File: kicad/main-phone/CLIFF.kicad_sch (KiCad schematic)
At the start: 14 parts, among them Q7304 AO3400

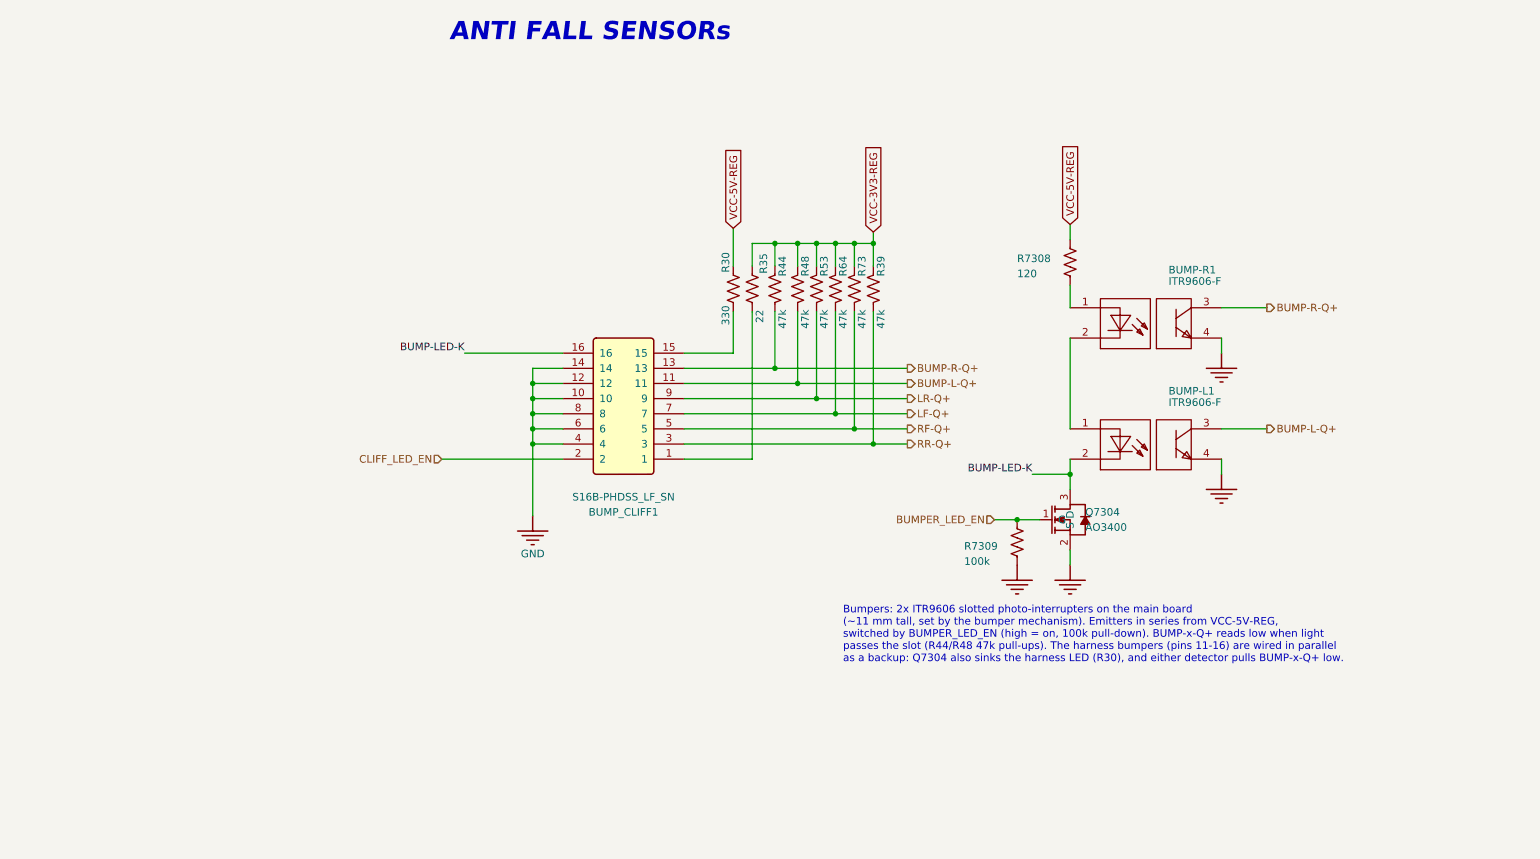
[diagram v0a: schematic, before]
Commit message: Cliff sensor board (IR333-A + PT333-3B, no lenses); main board drops the Roomba harness
- kicad/cliff-sensor: new board, fitted 6x. Narrow-beam 5 mm IR LED and black-lens
  phototransistor, 18 mm apart, tilted so the beams cross at the floor (tilt sets the
  reference distance). 150R LED resistor, SH 4-pin vertical (ZX-SH1.0-4PLT). Refs 85xx.
- main-phone CLIFF sheet: BUMP_CLIFF1 (Roomba 2x8 harness), R30, R35 removed; six SH 4-pin
  connectors CLIFF-LF1..RR1; Q7701 (AO3400) switches all cliff LEDs from CLIFF_LED_EN
  (R7703 pull-down); 47k pull-ups incl. new R7701/R7702 for cliff LM (PD9) / RM (PE8)
- STM32 sheet: PD9/PE8 carry cliff LM/RM (global labels), also on J7301 12/13
- JLCImport: IR333-A, PT333-3B, ZX-SH1_0-4PLT
- docs: cliff board README, SPEC, READMEs

Co-Authored-By: Claude Opus 5.5 <noreply@anthropic.com>
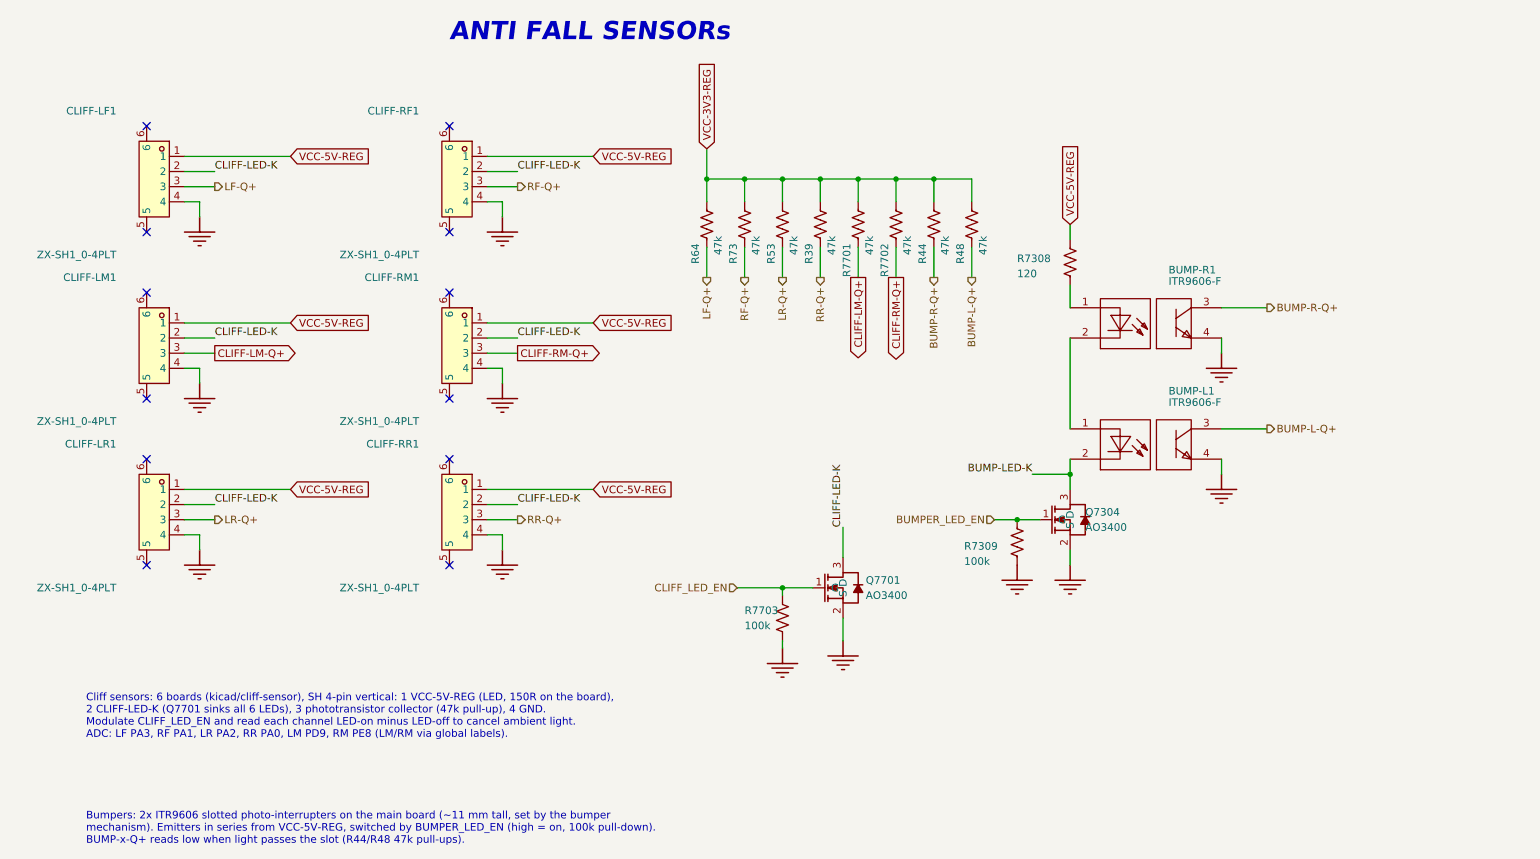
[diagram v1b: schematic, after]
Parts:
- removed BUMP_CLIFF1: S16B-PHDSS_LF_SN, JLCImport:S16B-PHDSS_LF_SN, symbol JLCImport:S16B-PHDSS_LF_SN
- removed R30: 330, Resistor_SMD:R_0603_1608Metric, symbol Device:R_US
- removed R35: 22, Resistor_SMD:R_0603_1608Metric, symbol Device:R_US
- added CLIFF-LF1, CLIFF-LM1, CLIFF-LR1, CLIFF-RF1, CLIFF-RM1, CLIFF-RR1: ZX-SH1_0-4PLT, JLCImport:ZX-SH1_0-4PLT, symbol JLCImport:ZX-SH1_0-4PLT
- added Q7701: AO3400, JLCImport:AO3400, symbol JLCImport:AO3400
- added R7701, R7702: 47k, Resistor_SMD:R_0603_1608Metric, symbol Device:R_US
- added R7703: 100k, Resistor_SMD:R_0603_1608Metric, symbol Device:R_US
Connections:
- net BUMP-L-Q+: now also R48.2; no longer R48.1
- net BUMP-R-Q+: now also R44.2; no longer R44.1
- net CLIFF_LED_EN: now also Q7701.1 (G), R7703.1
- net GND: now also CLIFF-LF1.4, CLIFF-LM1.4, CLIFF-LR1.4, CLIFF-RF1.4, CLIFF-RM1.4, CLIFF-RR1.4, Q7701.2 (S), R7703.2
- net LF-Q+: now also R64.2, CLIFF-LF1.3; no longer R64.1
- net LR-Q+: now also R53.2, CLIFF-LR1.3; no longer R53.1
- net RF-Q+: now also R73.2, CLIFF-RF1.3; no longer R73.1
- net RR-Q+: now also R39.2, CLIFF-RR1.3; no longer R39.1
- net VCC-3V3-REG: now also R39.1, R44.1, R48.1, R53.1, R64.1, R73.1, R7701.1, R7702.1; no longer R39.2, R44.2, R48.2, R53.2, R64.2, R73.2
- net VCC-5V-REG: now also CLIFF-LF1.1, CLIFF-LM1.1, CLIFF-LR1.1, CLIFF-RF1.1, CLIFF-RM1.1, CLIFF-RR1.1
- new net CLIFF-LED-K: CLIFF-LF1.2, CLIFF-LM1.2, CLIFF-LR1.2, CLIFF-RF1.2, CLIFF-RM1.2, CLIFF-RR1.2, Q7701.3 (D)
- new net CLIFF-LM-Q+: CLIFF-LM1.3, R7701.2
- new net CLIFF-RM-Q+: CLIFF-RM1.3, R7702.2
- no-connect marks 0 -> 12
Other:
- note added: "Bumpers: 2x ITR9606 slotted photo-interrupters on the main board (~11 mm tall, set by the bumper mechanism). Emitters in series from VCC-5V-REG, switched by BUMPER_LED_EN (high = on, 100k pull-down). BUMP-x-Q+ reads low when light passes the slot (R44/R48 47k pull-ups)."
- note added: "Cliff sensors: 6 boards (kicad/cliff-sensor), SH 4-pin vertical: 1 VCC-5V-REG (LED, 150R on the board), 2 CLIFF-LED-K (Q7701 sinks all 6 LEDs), 3 phototransistor collector (47k pull-up), 4 GND. Modulate CLIFF_LED_EN and read each channel LED-on minus LED-off to cancel ambient light. ADC: LF PA3, RF PA1, LR PA2, RR PA0, LM PD9, RM PE8 (LM/RM via global labels)."
- note removed: "Bumpers: 2x ITR9606 slotted photo-interrupters on the main board (~11 mm tall, set by the bumper mechanism). Emitters in series from VCC-5V-REG, switched by BUMPER_LED_EN (high = on, 100k pull-down). BUMP-x-Q+ reads low when light passes the slot (R44/R48 47k pull-ups). The harness bumpers (pins 11-16) are wired in parallel as a backup: Q7304 also sinks the harness LED (R30), and either detector 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"
